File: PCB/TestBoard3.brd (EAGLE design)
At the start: 62.2 x 36.8 mm, 29 parts, among them U1 PSSI2021SAY, U2 DS3502U+, U3 PDTC124XU, Y1 CC4V-T1A

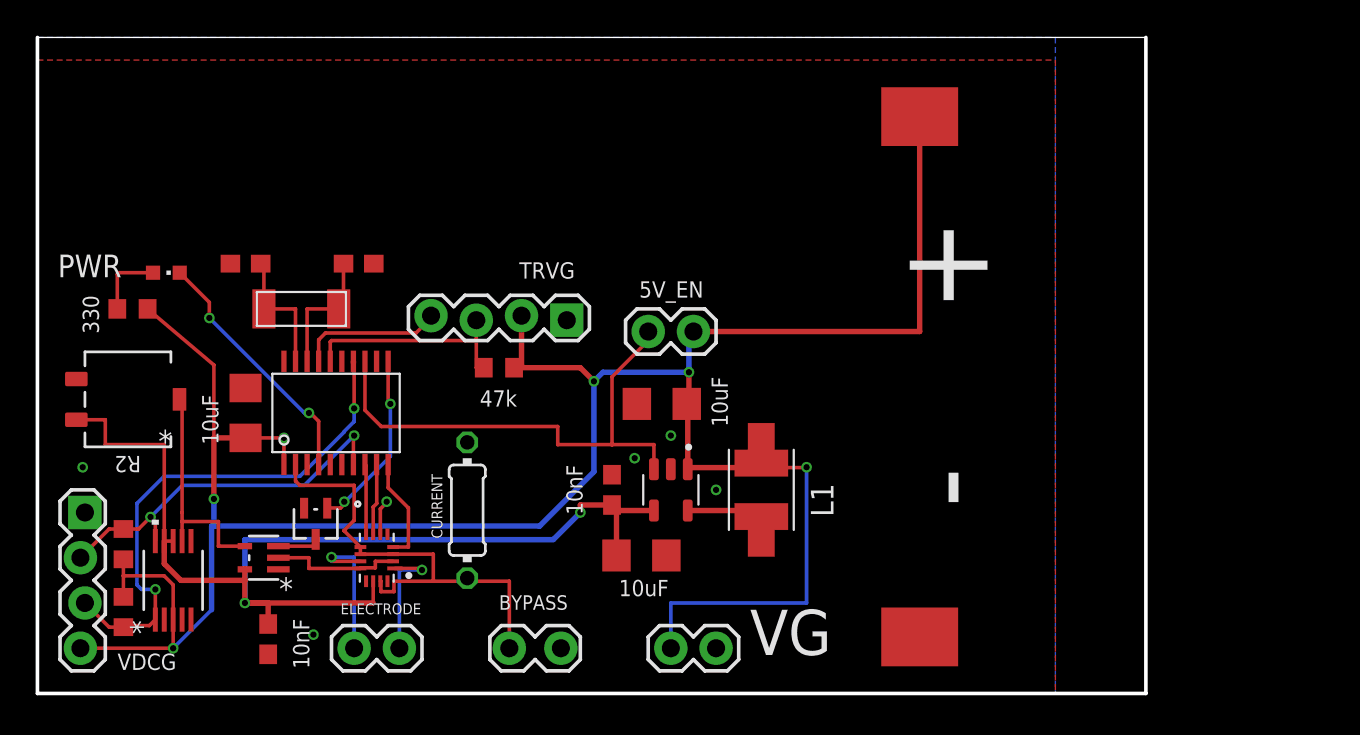
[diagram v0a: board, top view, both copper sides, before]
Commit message: Version 3 of PCB. OshPark manufactured version.
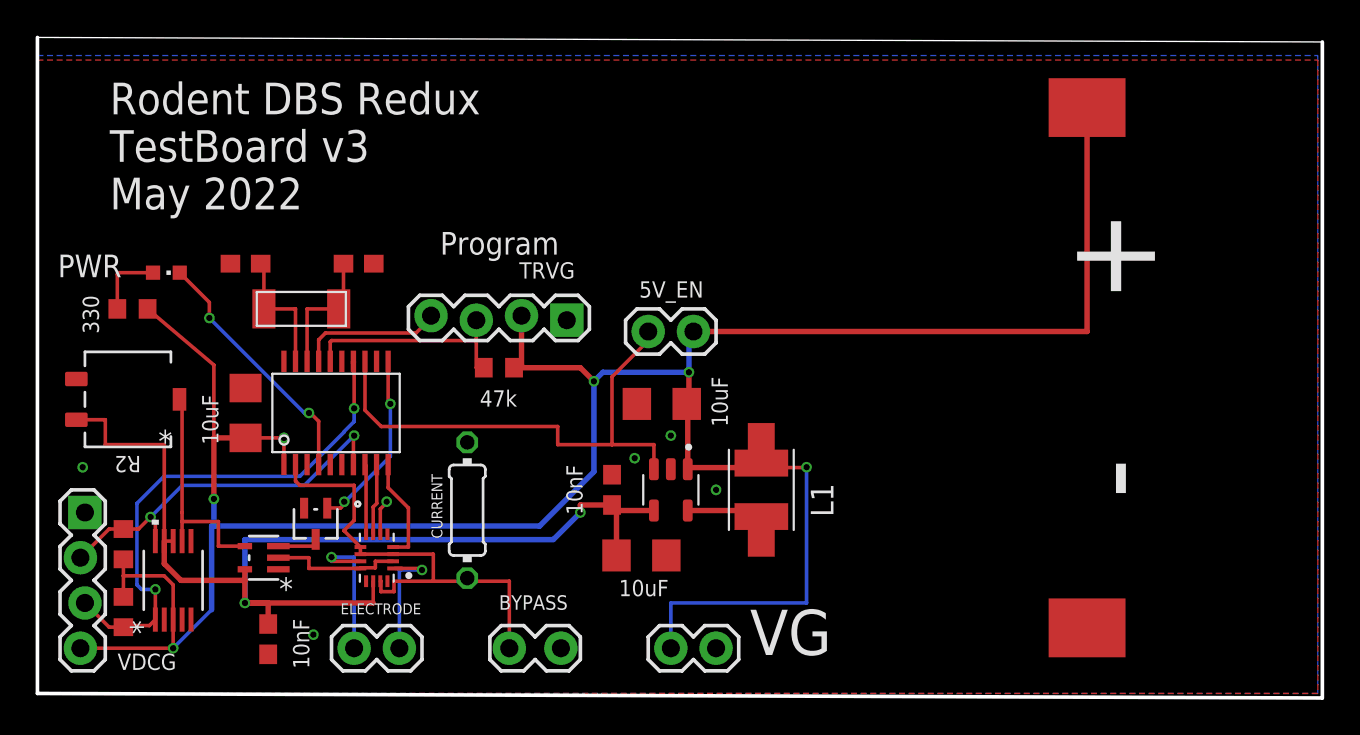
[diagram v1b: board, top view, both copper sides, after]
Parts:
- moved BAT1 9.41 mm to (58.9, 18.3)
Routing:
- net VDD: track 139.6 -> 149.5 mm
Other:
- board size 62.2 x 36.8 mm -> 72.1 x 37.1 mm
- board text added: "Caleb Kemere May 2022 sdg"
- board text added: "Program"
- board text added: "Rodent DBS Redux TestBoard v3 May 2022"
- board text removed: "TestBoard3 May 2022 sdg"
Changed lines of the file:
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@@
 <plain>
 <wire x1="0" y1="36.83" x2="0" y2="0" width="0.2032" layer="20"/>
-<wire x1="0" y1="0" x2="62.23" y2="0" width="0.2032" layer="20"/>
-<wire x1="62.23" y1="0" x2="62.23" y2="36.83" width="0.2032" layer="20"/>
-<wire x1="62.23" y1="36.83" x2="0" y2="36.83" width="0" layer="20"/>
-<text x="48.768" y="14.478" size="0.8128" layer="22" font="vector" ratio="15" rot="MR0">TestBoard3
+<wire x1="0" y1="0" x2="72.136" y2="-0.254" width="0.2032" layer="20"/>
+<wire x1="72.136" y1="-0.254" x2="72.136" y2="36.576" width="0.2032" layer="20"/>
+<wire x1="72.136" y1="36.576" x2="0" y2="36.83" width="0" layer="20"/>
+<text x="11.176" y="29.21" size="0.8128" layer="22" font="vector" ratio="15" rot="MR0">Caleb Kemere
 May 2022
 sdg</text>
+<text x="4.064" y="27.178" size="1.778" layer="21" font="vector" ratio="15">Rodent DBS Redux
+TestBoard v3
+May 2022</text>
+<text x="22.606" y="24.638" size="1.27" layer="21" font="vector" ratio="15">Program</text>
 </plain>
 <attributes>
@@
 <attribute name="PURCHASE-URL" value="https://www.digikey.com/en/products/detail/micro-crystal-ag/CC4V-T1A-32-768KHZ-7PF-20PPM-TA-QC/10499071" x="14.81405" y="21.59" size="1.778" layer="27" display="off"/>
 </element>
-<element name="BAT1" library="ELEC327" package="BU2032SM" value="" x="49.53" y="17.78" smashed="yes" rot="R270"/>
+<element name="BAT1" library="ELEC327" package="BU2032SM" value="" x="58.928" y="18.288" smashed="yes" rot="R270"/>
 <element name="VG" library="SparkFun-Connectors" library_urn="urn:adsk.eagle:library:513" package="1X02" package3d_urn="urn:adsk.eagle:package:38039/1" value="" x="38.1" y="2.54" smashed="yes" rot="R180">
 <attribute name="NAME" x="40.005" y="2.159" size="2.54" layer="25" font="vector" ratio="20"/>
@@
 <vertex x="0" y="0"/>
 <vertex x="0" y="35.56"/>
-<vertex x="57.15" y="35.56"/>
-<vertex x="57.15" y="0"/>
+<vertex x="71.882" y="35.56"/>
+<vertex x="71.882" y="0"/>
 </polygon>
 <polygon width="0.3048" layer="16">
 <vertex x="0" y="0"/>
-<vertex x="0" y="36.83"/>
-<vertex x="57.15" y="36.83"/>
-<vertex x="57.15" y="0"/>
+<vertex x="0" y="35.814"/>
+<vertex x="71.882" y="35.814"/>
+<vertex x="71.882" y="0"/>
 </polygon>
 <via x="38.1" y="11.43" extent="1-16" drill="0.35"/>
@@
 <wire x1="43.18" y1="12.7" x2="43.18" y2="12.68" width="0.2032" layer="1"/>
 <wire x1="43.18" y1="12.68" x2="40.64" y2="12.68" width="0.2032" layer="1"/>
-<wire x1="49.53" y1="32.385" x2="49.53" y2="20.32" width="0.3048" layer="1"/>
-<wire x1="49.53" y1="20.32" x2="36.83" y2="20.32" width="0.3048" layer="1"/>
+<wire x1="58.928" y1="32.893" x2="58.928" y2="20.32" width="0.3048" layer="1"/>
+<wire x1="58.928" y1="20.32" x2="36.83" y2="20.32" width="0.3048" layer="1"/>
 <wire x1="13.8391" y1="12.8479" x2="13.8391" y2="14.348" width="0.2032" layer="1"/>
 <wire x1="9.779" y1="4.699" x2="9.779" y2="9.398" width="0.3048" layer="16"/>
